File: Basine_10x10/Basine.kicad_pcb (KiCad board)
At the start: 2 copper layers, 100 x 100 mm, 74 parts, among them J1 2060-451/998-404, J10 2060-451/998-404, J11 2060-451/998-404, J12 2060-451/998-404, J13 2060-451/998-404, J14 2060-451/998-404, J15 2060-451/998-404, J16 2060-451/998-404, J2 2060-451/998-404, J3 2060-451/998-404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

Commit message: Basine_10x10 :
ajout ultrogothe
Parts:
- removed C5, C6: 1uF, Capacitor_SMD:C_0402_1005Metric
- removed D4: 1N5819WS, Diode_SMD:D_SOD-323
- removed D5: LED, LED_SMD:LED_0603_1608Metric
- removed R7: 10k, Resistor_SMD:R_0603_1608Metric
- removed U3: XC6206PxxxMR, Package_TO_SOT_SMD:SOT-23-3
- added JP10: SolderJumper_2_Open, Jumper:SolderJumper-2_P1.3mm_Open_TrianglePad1.0x1.5mm, B.Cu at (87.1, 149.8)
- added JP11: SolderJumper_2_Open, Jumper:SolderJumper-2_P1.3mm_Open_TrianglePad1.0x1.5mm, B.Cu at (82.7, 142.7)
- added JP12: SolderJumper_2_Open, Jumper:SolderJumper-2_P1.3mm_Open_TrianglePad1.0x1.5mm, B.Cu at (82.7, 146.3)
- added JP13: SolderJumper_2_Open, Jumper:SolderJumper-2_P1.3mm_Open_TrianglePad1.0x1.5mm, B.Cu at (82.7, 149.8)
- added JP14: SolderJumper_2_Open, Jumper:SolderJumper-2_P1.3mm_Open_TrianglePad1.0x1.5mm, B.Cu at (78.4, 142.7)
- added JP15: SolderJumper_2_Open, Jumper:SolderJumper-2_P1.3mm_Open_TrianglePad1.0x1.5mm, B.Cu at (78.4, 146.3)
- added JP16: SolderJumper_2_Open, Jumper:SolderJumper-2_P1.3mm_Open_TrianglePad1.0x1.5mm, B.Cu at (78.4, 149.8)
- added JP5: SolderJumper_2_Open, Jumper:SolderJumper-2_P1.3mm_Open_TrianglePad1.0x1.5mm, B.Cu at (91.4, 142.7)
- added JP6: SolderJumper_2_Open, Jumper:SolderJumper-2_P1.3mm_Open_TrianglePad1.0x1.5mm, B.Cu at (91.4, 146.3)
- added JP7: SolderJumper_2_Open, Jumper:SolderJumper-2_P1.3mm_Open_TrianglePad1.0x1.5mm, B.Cu at (91.4, 149.8)
- added JP8: SolderJumper_2_Open, Jumper:SolderJumper-2_P1.3mm_Open_TrianglePad1.0x1.5mm, B.Cu at (87.1, 142.7)
- added JP9: SolderJumper_2_Open, Jumper:SolderJumper-2_P1.3mm_Open_TrianglePad1.0x1.5mm, B.Cu at (87.1, 146.3)
- added TP1: TestPoint, Chimere_comps:Pastille, F.Cu at (129.7, 157.6)
- added TP10: TestPoint, Chimere_comps:Pastille, F.Cu at (86.0, 153.0)
- added TP11: TestPoint, Chimere_comps:Pastille, F.Cu at (86.0, 155.8)
- added TP12: TestPoint, Chimere_comps:Pastille, F.Cu at (86.0, 158.6)
- added TP2: TestPoint, Chimere_comps:Pastille, F.Cu at (77.6, 155.8)
- added TP3: TestPoint, Chimere_comps:Pastille, F.Cu at (77.6, 158.6)
- added TP4: TestPoint, Chimere_comps:Pastille, F.Cu at (80.4, 153.0)
- added TP5: TestPoint, Chimere_comps:Pastille, F.Cu at (80.4, 155.8)
- added TP6: TestPoint, Chimere_comps:Pastille, F.Cu at (80.4, 158.6)
- added TP7: TestPoint, Chimere_comps:Pastille, F.Cu at (83.2, 153.0)
- added TP8: TestPoint, Chimere_comps:Pastille, F.Cu at (83.2, 155.8)
- added TP9: TestPoint, Chimere_comps:Pastille, F.Cu at (83.2, 158.6)
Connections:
- U10 pad 4: unconnected-(U10-IO_i-Pad4) -> Net-(JP10-B)
- U11 pad 4: unconnected-(U11-IO_i-Pad4) -> Net-(JP11-B)
- U12 pad 4: unconnected-(U12-IO_i-Pad4) -> Net-(JP12-B)
- U13 pad 4: unconnected-(U13-IO_i-Pad4) -> Net-(JP13-B)
- U14 pad 4: unconnected-(U14-IO_i-Pad4) -> Net-(JP14-B)
- U15 pad 4: unconnected-(U15-IO_i-Pad4) -> Net-(JP15-B)
- U16 pad 4: unconnected-(U16-IO_i-Pad4) -> Net-(JP16-B)
- U5 pad 4: unconnected-(U5-IO_i-Pad4) -> Net-(JP5-B)
- U6 pad 4: unconnected-(U6-IO_i-Pad4) -> Net-(JP6-B)
- U7 pad 4: unconnected-(U7-IO_i-Pad4) -> Net-(JP7-B)
- U8 pad 4: unconnected-(U8-IO_i-Pad4) -> Net-(JP8-B)
- U9 pad 4: unconnected-(U9-IO_i-Pad4) -> Net-(JP9-B)
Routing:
- net Net-(D4-K): track 6.20 -> 0.00 mm
- net (no net): track 7.67 -> 13.9 mm
- net 5V: track 38.5 -> 42.6 mm
- net 3V3: track 7.84 -> 3.67 mm
- net Net-(D5-A): track 1.80 -> 0.00 mm
- net /s_ALIM_5V/Vsense: track 0.00 -> 1.80 mm

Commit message: Basine_10x10
ajout symbole ultrogothe
ajout power flag sur 5V
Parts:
- added JP17: SolderJumper_2_Open, Jumper:SolderJumper-2_P1.3mm_Open_TrianglePad1.0x1.5mm, F.Cu at (67.7, 155.8)
- added JP18: SolderJumper_2_Open, Jumper:SolderJumper-2_P1.3mm_Open_TrianglePad1.0x1.5mm, F.Cu at (71.3, 155.8)
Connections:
- JP10 pad 1: unconnected-(JP10-A-Pad1) -> A6
- JP11 pad 1: unconnected-(JP11-A-Pad1) -> A5
- JP12 pad 1: unconnected-(JP12-A-Pad1) -> A4
- JP13 pad 1: unconnected-(JP13-A-Pad1) -> A3
- JP14 pad 1: unconnected-(JP14-A-Pad1) -> A2
- JP15 pad 1: unconnected-(JP15-A-Pad1) -> A1
- JP16 pad 1: unconnected-(JP16-A-Pad1) -> A0
- JP5 pad 1: unconnected-(JP5-A-Pad1) -> B10
- JP6 pad 1: unconnected-(JP6-A-Pad1) -> B2
- JP7 pad 1: unconnected-(JP7-A-Pad1) -> B1
- JP8 pad 1: unconnected-(JP8-A-Pad1) -> B0
- JP9 pad 1: unconnected-(JP9-A-Pad1) -> A7

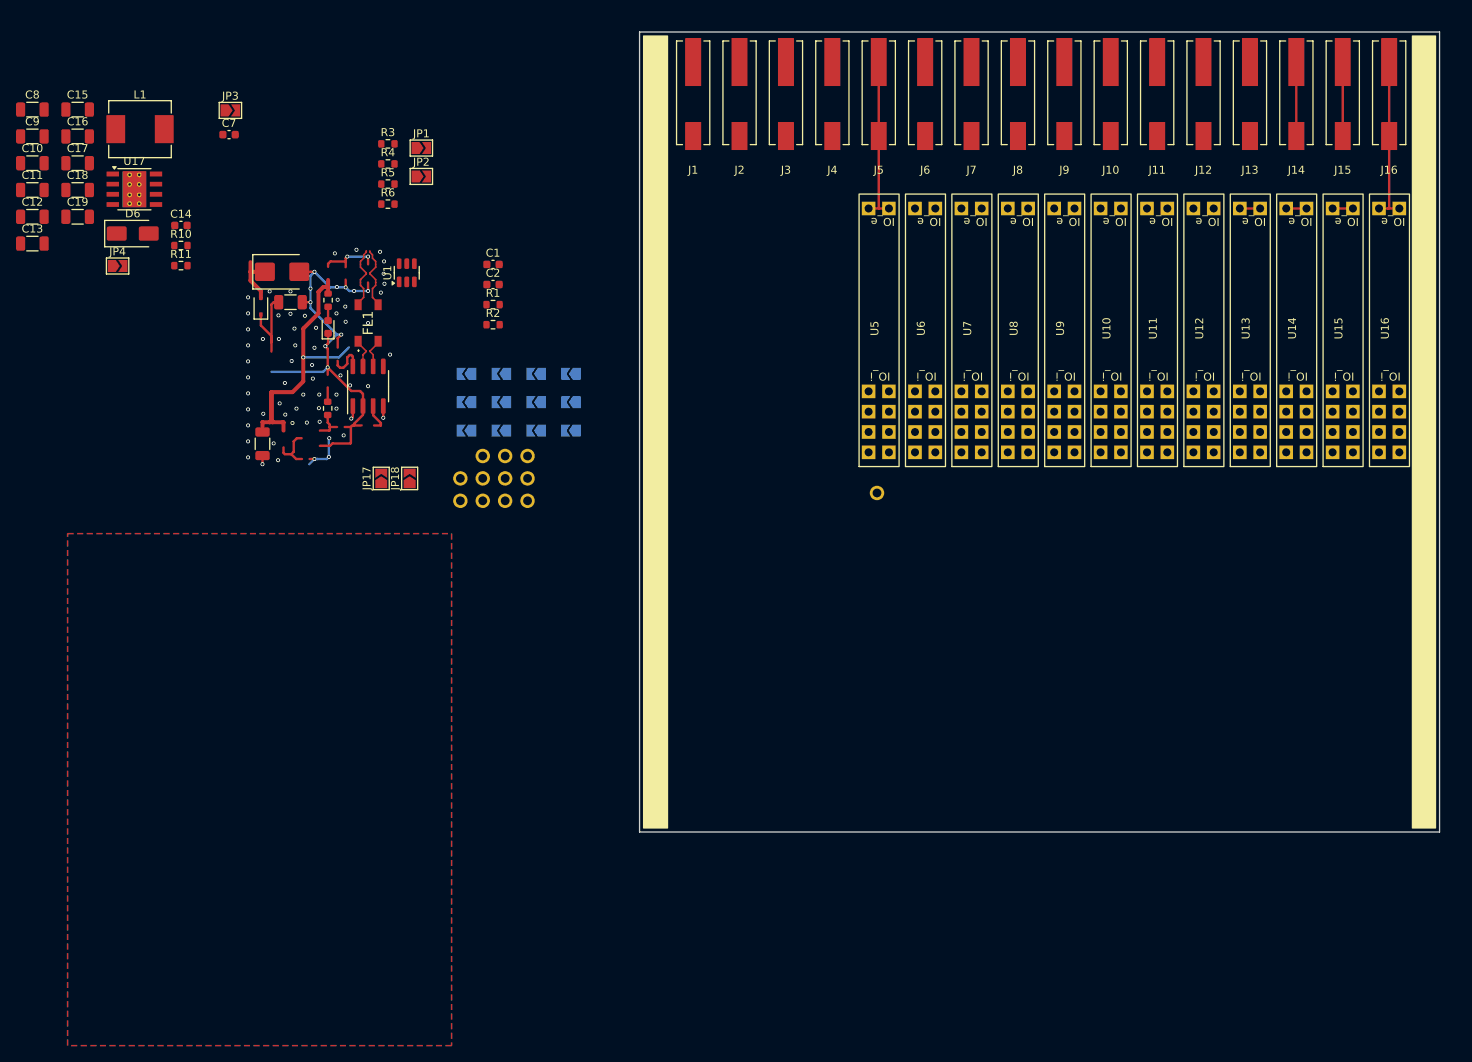
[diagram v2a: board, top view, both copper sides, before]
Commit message: 10x10
 ajout empreinte ultrogothe
placement ultrogothe et un peu alim 5V
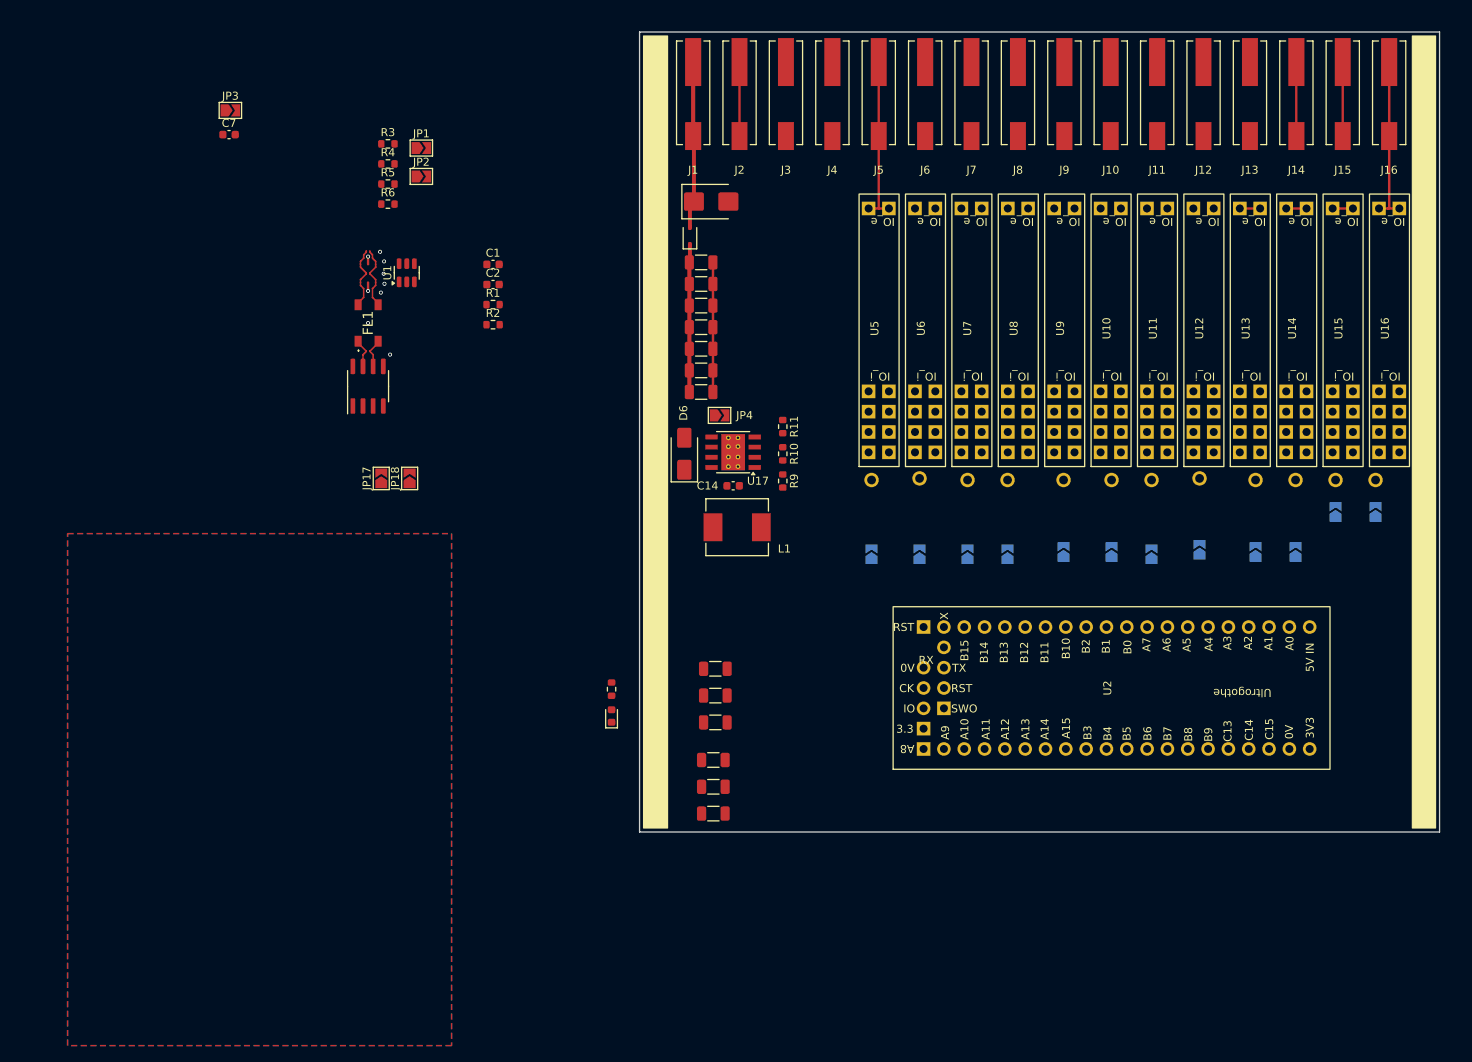
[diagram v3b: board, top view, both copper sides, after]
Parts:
- added U2: ~, Chimere_mods:Ultrogothe, F.Cu at (159.0, 182.0)
- moved JP16 114.1 mm to (192.0, 160.0), turned to 90 degrees
- moved C11 111.0 mm to (109.2, 191.0)
- moved C12 111.0 mm to (109.2, 194.3)
- moved C13 111.0 mm to (109.2, 197.7)
- moved JP15 109.5 mm to (187.0, 160.0), turned to 90 degrees
- moved TP12 106.0 mm to (192.0, 156.0)
- moved C15 106.0 mm to (109.5, 179.6)
- moved C16 106.0 mm to (109.5, 182.9)
- moved C17 106.0 mm to (109.5, 186.3)
- moved JP14 106.0 mm to (182.0, 165.0), turned to 90 degrees
- moved TP11 101.0 mm to (187.0, 156.0)
- moved TP10 96.0 mm to (182.0, 156.0)
- moved JP13 95.5 mm to (177.0, 165.0), turned to 90 degrees
- moved TP9 93.8 mm to (177.0, 156.0)
- moved L1 89.7 mm to (112.2, 161.9)
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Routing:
- net 5V: track 42.6 -> 0.00 mm, vias 1 -> 0
- net 0V: track 64.8 -> 26.5 mm, vias 71 -> 8
- net 24V: track 6.79 -> 20.9 mm
- net (no net): track 13.9 -> 0.96 mm, vias 2 -> 1
- net /s_ALIM_5V/Vs_f: track 10.9 -> 18.5 mm
- net Net-(U4-Rs): track 5.04 -> 0.00 mm
- net 3V3: track 3.67 -> 0.00 mm
- net /s_ALIM_5V/Vsense: track 1.80 -> 0.00 mm
- net Net-(D3-A): track 1.74 -> 0.00 mm
- net CAN_TX: track 1.66 -> 0.00 mm, vias 1 -> 0
- net CAN_RX: track 1.48 -> 0.01 mm, vias 1 -> 0

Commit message: 10x10
placement et routage du CAN
divers
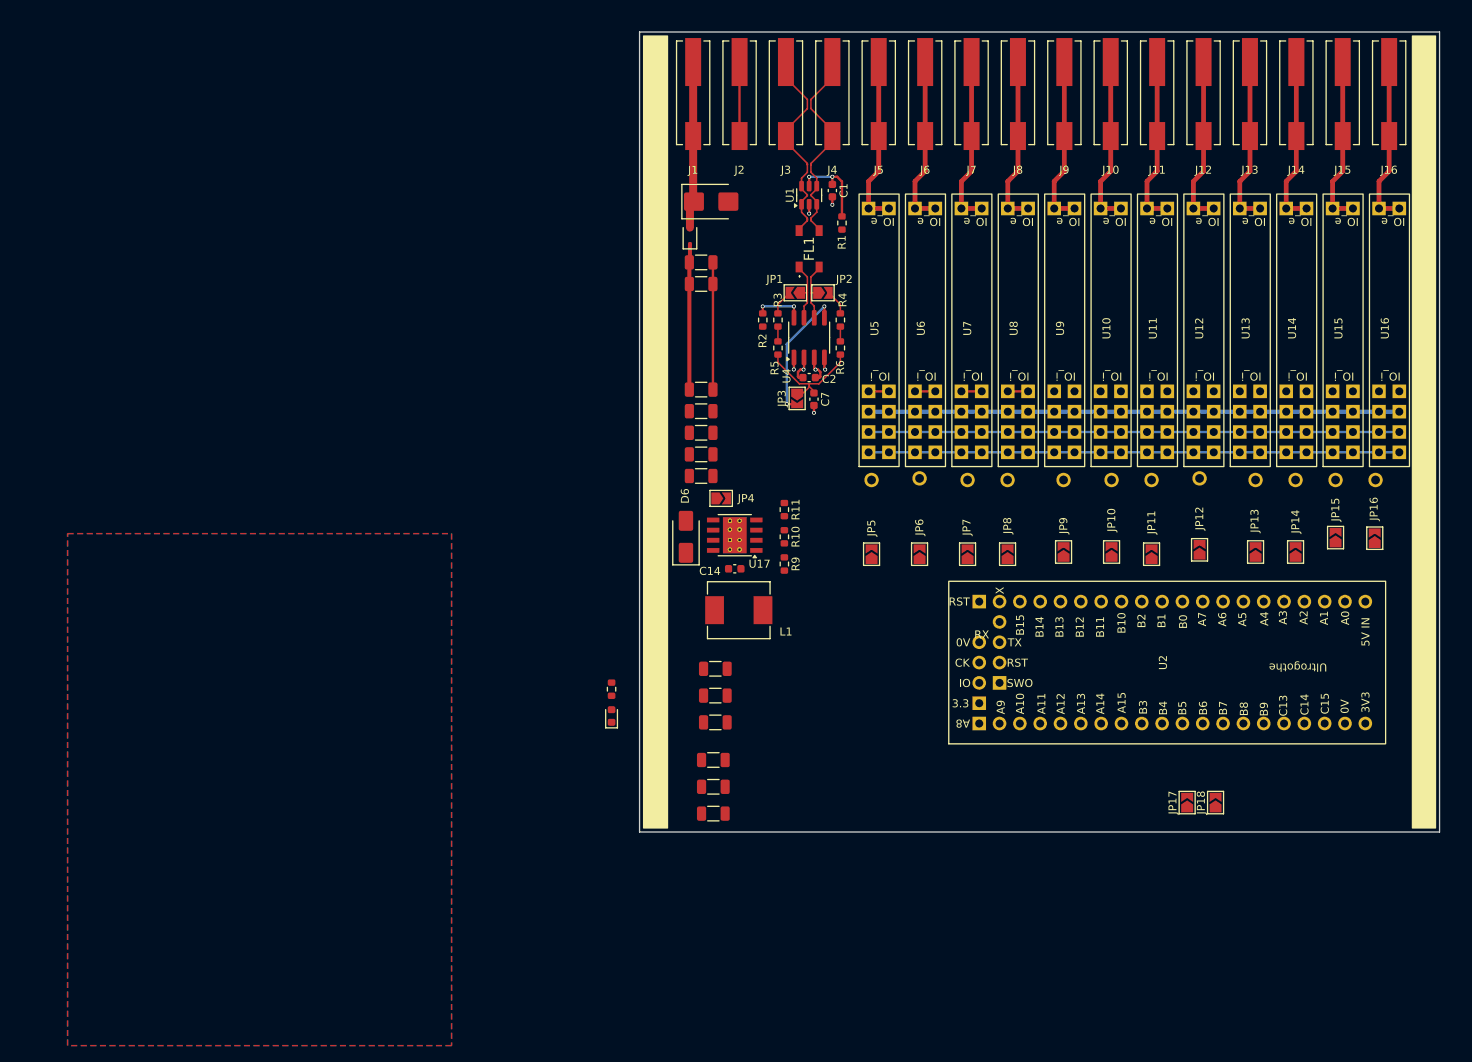
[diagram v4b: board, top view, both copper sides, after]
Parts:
- JP10, JP11, JP12, JP13, JP14, JP15, JP16, JP5, JP6, JP7, JP8, JP9: moved to F.Cu
- moved JP17 108.6 mm to (168.4, 196.3)
- moved JP18 108.6 mm to (172.0, 196.3)
- moved C7 80.2 mm to (121.8, 145.9), turned to -90 degrees
- moved JP3 79.5 mm to (119.7, 145.8), turned to -90 degrees
- moved R4 59.8 mm to (125.1, 136.0), turned to -90 degrees
- moved R6 59.3 mm to (125.1, 139.5), turned to -90 degrees
- moved FL1 55.9 mm to (121.2, 127.1)
- moved U4 55.5 mm to (121.2, 138.2)
- moved R3 53.5 mm to (117.3, 136.0), turned to -90 degrees
- moved R5 52.9 mm to (117.3, 139.5), turned to -90 degrees
- moved JP2 52.3 mm to (122.9, 132.6)
- moved U1 51.2 mm to (121.2, 120.4)
- moved JP1 50.1 mm to (119.5, 132.6), turned to 180 degrees
- moved R1 44.8 mm to (125.3, 123.9), turned to -90 degrees
- moved C1 43.4 mm to (124.1, 119.8), turned to -90 degrees
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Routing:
- net 0V: track 26.5 -> 98.5 mm, vias 8 -> 4
- net 3V3: track 0.00 -> 70.0 mm, vias 0 -> 1
- net 5V: track 0.00 -> 66.3 mm
- net Net-(J7-Pin_1): track 0.00 -> 21.4 mm
- net Net-(J12-Pin_1): track 0.00 -> 21.4 mm
- net Net-(J8-Pin_1): track 0.00 -> 21.4 mm
- net Net-(J10-Pin_1): track 0.00 -> 21.4 mm
- net Net-(J9-Pin_1): track 0.00 -> 21.4 mm
- net Net-(J6-Pin_1): track 0.00 -> 21.4 mm
- net Net-(J11-Pin_1): track 0.00 -> 21.4 mm
- net Net-(J13-Pin_1): track 2.54 -> 21.4 mm
- net CAN_N: track 8.13 -> 26.3 mm
- net CAN_P: track 8.13 -> 26.3 mm
- net /s_CAN/Vref_can: track 0.00 -> 16.8 mm, vias 0 -> 2
- net /s_CAN/can_milieu: track 0.00 -> 15.2 mm
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
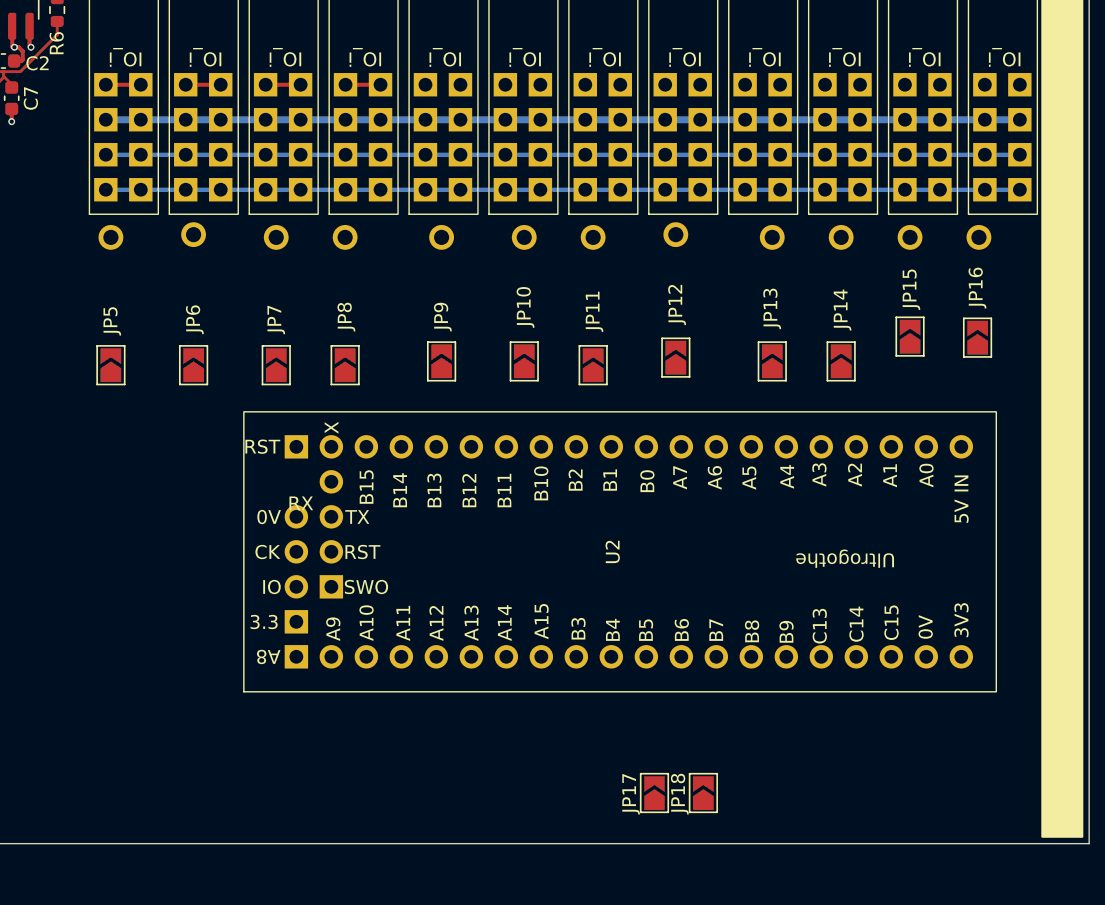
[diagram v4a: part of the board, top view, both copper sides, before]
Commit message: Update Basine.kicad_pcb
alignement et routage des jumpers
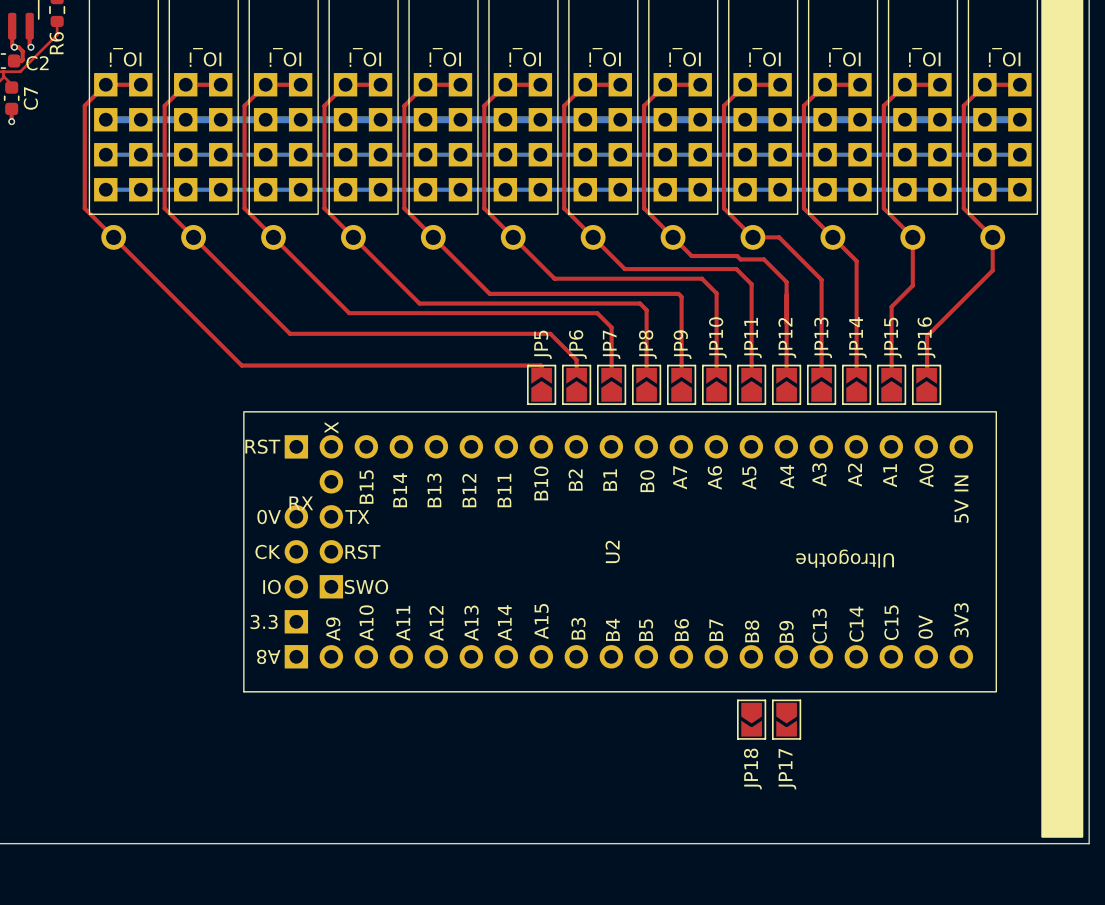
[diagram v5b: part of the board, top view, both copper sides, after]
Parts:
- moved JP5 31.3 mm to (160.3, 166.7)
- moved JP6 27.8 mm to (162.8, 166.7)
- moved JP7 24.4 mm to (165.3, 166.7)
- moved JP8 21.9 mm to (167.9, 166.7)
- moved JP9 17.5 mm to (170.4, 166.7)
- moved JP10 14.1 mm to (173.0, 166.7)
- moved JP11 11.6 mm to (175.5, 166.7)
- moved JP17 11.0 mm to (178.0, 191.0), turned to -90 degrees
- moved JP12 8.28 mm to (178.0, 166.7)
- moved JP18 6.37 mm to (175.5, 191.0), turned to -90 degrees
- moved JP16 5.04 mm to (188.2, 166.7)
- moved JP13 3.96 mm to (180.6, 166.7)
- moved JP15 3.75 mm to (185.7, 166.7)
- moved JP14 2.04 mm to (183.1, 166.7)
- moved TP9 1.40 mm to (175.6, 156.0)
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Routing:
- net Net-(JP5-B): track 2.54 -> 50.7 mm
- net Net-(JP6-B): track 2.54 -> 47.7 mm
- net Net-(JP7-B): track 2.54 -> 45.8 mm
- net Net-(JP8-B): track 2.54 -> 43.3 mm
- net Net-(JP9-B): track 0.00 -> 40.6 mm
- net Net-(JP10-B): track 0.00 -> 37.5 mm
- net Net-(JP11-B): track 0.00 -> 34.6 mm
- net Net-(JP12-B): track 0.00 -> 33.5 mm
- net Net-(JP13-B): track 0.00 -> 28.3 mm
- net Net-(JP16-B): track 0.00 -> 27.1 mm
- net Net-(JP14-B): track 0.00 -> 25.8 mm
- net Net-(JP15-B): track 0.00 -> 25.7 mm
